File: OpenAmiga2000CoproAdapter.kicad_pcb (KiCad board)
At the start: 2 copper layers, 188.6 x 110.4 mm, 74 parts, among them CN1 A2000_COPRO_SLOT, P1 CONN_2, P10 CONN_1, P11 CONN_1, P12 CONN_1, P13 CONN_1, P14 CONN_1, P15 CONN_1, P2 CONN_2, P3 CONN_2, P4 CONN_2, P5 CONN_1, P6 CONN_1, P7 CONN_1, P8 CONN_1, P9 CONN_1, P99 OSHW_LOGO, U1 68000D, U10 Spare, U11 74HCT00, U12 74HCT27, U13 74HCT74, U14 74F86, U15 74F74, U16 74HCT04, U17 74HCT112, U18 74F157, U19 74F157, U2 AS6C4008-55PCN, U3 AS6C4008-55PCN, U4 AS6C4008-55PCN, U5 AS6C4008-55PCN, U6 74HCT00, U7 74HCT32, U8 74HCT32, U9 74LS05

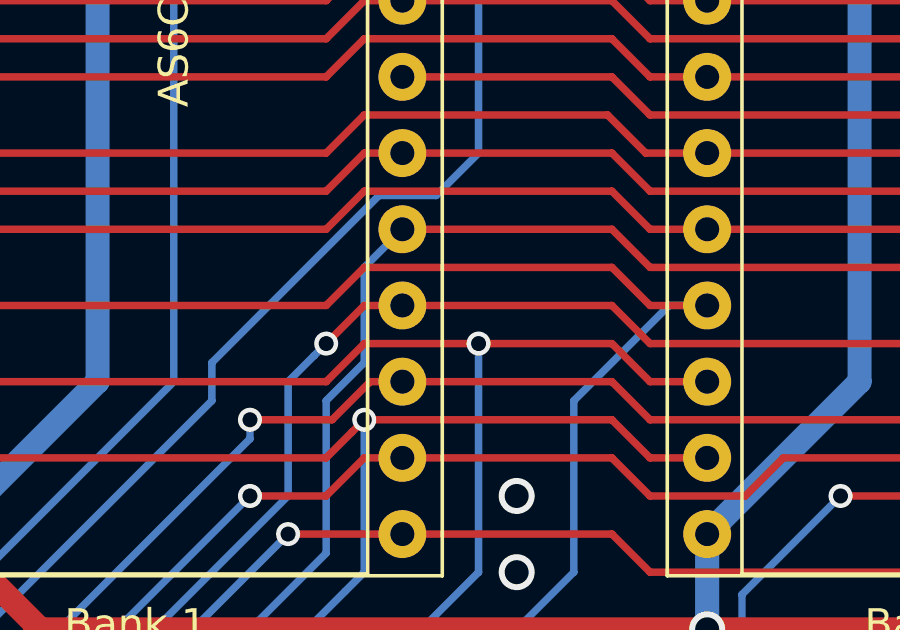
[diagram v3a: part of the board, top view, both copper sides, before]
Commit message: remove via
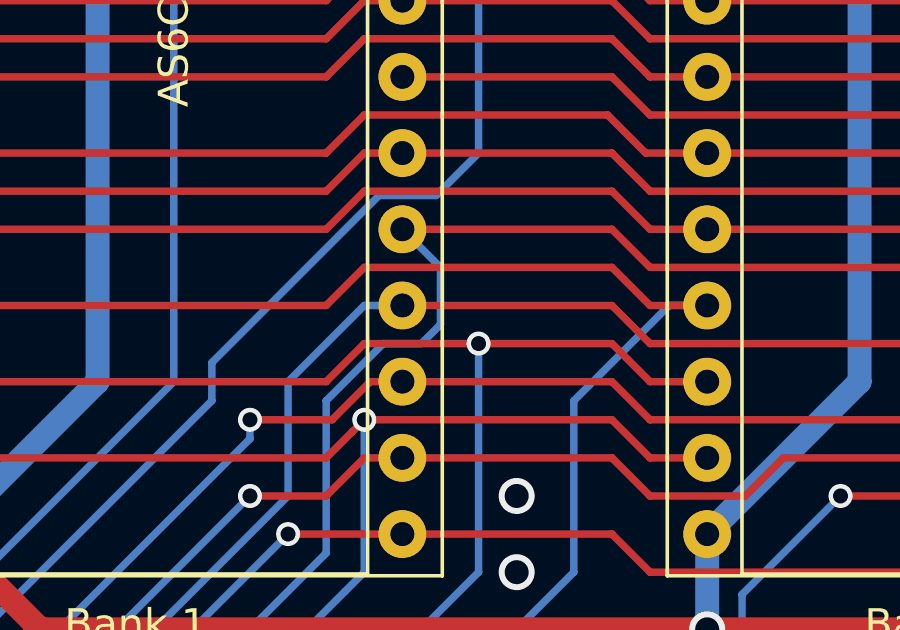
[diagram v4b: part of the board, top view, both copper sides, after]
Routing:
- net /d7: track 89.9 -> 91.7 mm
- net /d6: vias 2 -> 1
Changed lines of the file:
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@@
   (segment (start 95.758 139.1845) (end 95.758 134.9375) (width 0.25) (layer F.Cu) (net 60) (status 20))
   (segment (start 95.758 142.6845) (end 95.758 139.1845) (width 0.25) (layer F.Cu) (net 60) (status 10))
-  (via (at 100.901502 86.36) (size 0.8) (drill 0.5) (layers F.Cu B.Cu) (net 60))
-  (segment (start 99.6315 87.630002) (end 100.501503 86.759999) (width 0.25) (layer B.Cu) (net 60))
-  (segment (start 99.6315 91.44) (end 99.6315 87.630002) (width 0.25) (layer B.Cu) (net 60))
-  (segment (start 100.501503 86.759999) (end 100.901502 86.36) (width 0.25) (layer B.Cu) (net 60))
-  (segment (start 94.53299 96.53851) (end 99.6315 91.44) (width 0.25) (layer B.Cu) (net 60))
-  (segment (start 94.53299 97.17351) (end 94.53299 96.53851) (width 0.25) (layer B.Cu) (net 60))
   (via (at 94.53299 97.17351) (size 0.8) (drill 0.5) (layers F.Cu B.Cu) (net 60))
   (segment (start 95.758 115.5065) (end 95.758 134.9375) (width 0.25) (layer F.Cu) (net 60))
   (segment (start 94.53299 114.28149) (end 95.758 115.5065) (width 0.25) (layer F.Cu) (net 60))
   (segment (start 94.53299 97.17351) (end 94.53299 114.28149) (width 0.25) (layer F.Cu) (net 60))
-  (segment (start 102.171502 85.09) (end 100.901502 86.36) (width 0.25) (layer F.Cu) (net 60))
-  (segment (start 110.4265 85.09) (end 102.171502 85.09) (width 0.25) (layer F.Cu) (net 60))
-  (segment (start 111.6965 86.36) (end 110.4265 85.09) (width 0.25) (layer F.Cu) (net 60))
-  (segment (start 127.5715 86.36) (end 111.6965 86.36) (width 0.25) (layer F.Cu) (net 60))
-  (segment (start 128.8415 85.09) (end 127.5715 86.36) (width 0.25) (layer F.Cu) (net 60))
   (segment (start 98.298 139.1845) (end 98.298 134.9375) (width 0.25) (layer F.Cu) (net 61) (status 20))
   (segment (start 98.298 142.6845) (end 98.298 139.1845) (width 0.25) (layer F.Cu) (net 61) (status 10))
-  (segment (start 102.1715 86.995) (end 102.1715 83.82) (width 0.25) (layer B.Cu) (net 61))
-  (segment (start 100.9015 88.265) (end 102.1715 86.995) (width 0.25) (layer B.Cu) (net 61))
-  (segment (start 100.9015 93.345) (end 100.9015 88.265) (width 0.25) (layer B.Cu) (net 61))
   (segment (start 96.98301 97.26349) (end 97.0915 97.155) (width 0.25) (layer B.Cu) (net 61))
-  (segment (start 102.1715 83.82) (end 103.4415 82.55) (width 0.25) (layer B.Cu) (net 61))
-  (segment (start 97.0915 97.155) (end 100.9015 93.345) (width 0.25) (layer B.Cu) (net 61))
   (via (at 97.0915 97.155) (size 0.8) (drill 0.5) (layers F.Cu B.Cu) (net 61))
   (segment (start 98.298 115.5065) (end 98.298 134.9375) (width 0.25) (layer F.Cu) (net 61))
@@
   (segment (start 187.8965 40.005) (end 64.7065 40.005) (width 0.25) (layer B.Cu) (net 58))
   (segment (start 57.0865 81.025002) (end 59.246498 83.185) (width 0.25) (layer B.Cu) (net 58))
+  (segment (start 110.4265 85.09) (end 103.4415 85.09) (width 0.25) (layer F.Cu) (net 60))
+  (segment (start 111.6965 86.36) (end 110.4265 85.09) (width 0.25) (layer F.Cu) (net 60))
+  (segment (start 127.5715 86.36) (end 111.6965 86.36) (width 0.25) (layer F.Cu) (net 60))
+  (segment (start 128.8415 85.09) (end 127.5715 86.36) (width 0.25) (layer F.Cu) (net 60))
+  (segment (start 102.171502 85.09) (end 103.4415 85.09) (width 0.25) (layer B.Cu) (net 60))
+  (segment (start 99.6315 87.630002) (end 102.171502 85.09) (width 0.25) (layer B.Cu) (net 60))
+  (segment (start 99.6315 91.44) (end 99.6315 87.630002) (width 0.25) (layer B.Cu) (net 60))
+  (segment (start 94.53299 96.53851) (end 99.6315 91.44) (width 0.25) (layer B.Cu) (net 60))
+  (segment (start 94.53299 97.17351) (end 94.53299 96.53851) (width 0.25) (layer B.Cu) (net 60))
+  (segment (start 104.7115 83.82) (end 103.4415 82.55) (width 0.25) (layer B.Cu) (net 61))
+  (segment (start 104.0765 86.36) (end 104.7115 85.725) (width 0.25) (layer B.Cu) (net 61))
+  (segment (start 102.8065 86.36) (end 104.0765 86.36) (width 0.25) (layer B.Cu) (net 61))
+  (segment (start 100.9015 88.265) (end 102.8065 86.36) (width 0.25) (layer B.Cu) (net 61))
+  (segment (start 104.7115 85.725) (end 104.7115 83.82) (width 0.25) (layer B.Cu) (net 61))
+  (segment (start 100.9015 93.345) (end 100.9015 88.265) (width 0.25) (layer B.Cu) (net 61))
+  (segment (start 97.0915 97.155) (end 100.9015 93.345) (width 0.25) (layer B.Cu) (net 61))
   (via (at 135.1915 98.425) (size 0.8) (drill 0.5) (layers F.Cu B.Cu) (net 64))
   (segment (start 139.0015 87.63) (end 135.1915 91.44) (width 0.25) (layer B.Cu) (net 64))

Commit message: move track
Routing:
- net GND: vias 128 -> 130
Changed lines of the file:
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@@
     (thickness 1.6)
     (drawings 124)
-    (tracks 2292)
+    (tracks 2295)
     (zones 0)
     (modules 74)
@@
   (via (at 108.5215 109.22) (size 1.2) (drill 0.8) (layers F.Cu B.Cu) (net 1))
   (via (at 105.9815 100.965) (size 1.2) (drill 0.8) (layers F.Cu B.Cu) (net 1))
-  (via (at 105.9815 109.855) (size 1.2) (drill 0.8) (layers F.Cu B.Cu) (net 1))
+  (via (at 105.9815 109.22) (size 1.2) (drill 0.8) (layers F.Cu B.Cu) (net 1))
   (via (at 144.0815 95.885) (size 1.2) (drill 0.8) (layers F.Cu B.Cu) (net 1))
   (via (at 141.5415 95.885) (size 1.2) (drill 0.8) (layers F.Cu B.Cu) (net 1))
@@
   (via (at 144.0815 127.635) (size 1.2) (drill 0.8) (layers F.Cu B.Cu) (net 1))
   (via (at 141.5415 130.175) (size 1.2) (drill 0.8) (layers F.Cu B.Cu) (net 1))
-  (via (at 136.4615 107.95) (size 1.2) (drill 0.8) (layers F.Cu B.Cu) (net 1))
+  (via (at 133.9215 109.22) (size 1.2) (drill 0.8) (layers F.Cu B.Cu) (net 1))
   (via (at 213.9315 103.505) (size 1.2) (drill 0.8) (layers F.Cu B.Cu) (net 1))
   (segment (start 213.9315 62.23) (end 213.9315 62.795685) (width 0.8) (layer B.Cu) (net 1))
@@
   (via (at 224.0915 47.625) (size 1.2) (drill 0.8) (layers F.Cu B.Cu) (net 1))
   (via (at 224.7265 71.12) (size 1.2) (drill 0.8) (layers F.Cu B.Cu) (net 1))
+  (via (at 136.4615 108.585) (size 0.8) (drill 0.5) (layers F.Cu B.Cu) (net 1))
+  (via (at 116.1415 109.22) (size 1.2) (drill 0.8) (layers F.Cu B.Cu) (net 1))
   (via (at 118.0465 91.44) (size 0.8) (drill 0.5) (layers F.Cu B.Cu) (net 127))
   (segment (start 131.318 134.9375) (end 131.318 131.806498) (width 0.8) (layer F.Cu) (net 2))
@@
   (via (at 152.9715 106.68) (size 0.8) (drill 0.5) (layers F.Cu B.Cu) (net 74))
   (segment (start 151.7015 85.09) (end 151.7015 105.41) (width 0.25) (layer B.Cu) (net 74))
-  (segment (start 118.64448 106.68) (end 152.9715 106.68) (width 0.25) (layer F.Cu) (net 74))
-  (segment (start 117.39299 107.93149) (end 118.64448 106.68) (width 0.25) (layer F.Cu) (net 74))
+  (segment (start 118.00948 107.315) (end 152.3365 107.315) (width 0.25) (layer F.Cu) (net 74))
+  (segment (start 152.3365 107.315) (end 152.9715 106.68) (width 0.25) (layer F.Cu) (net 74))
+  (segment (start 117.39299 107.93149) (end 118.00948 107.315) (width 0.25) (layer F.Cu) (net 74))
   (segment (start 117.39299 113.64649) (end 117.39299 107.93149) (width 0.25) (layer F.Cu) (net 74))
   (segment (start 118.618 114.8715) (end 117.39299 113.64649) (width 0.25) (layer F.Cu) (net 74))

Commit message: description
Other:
- board text added: "Amiga 2000 14MHz Accelerator 2MB Fast RAM / ROM Emulation"
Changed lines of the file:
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@@
   (general
     (thickness 1.6)
-    (drawings 124)
+    (drawings 125)
     (tracks 2295)
     (zones 0)
@@
       (net 111 +12V))
   )
-  (gr_text "Little Turbo" (at 118.0465 38.1) (layer F.SilkS)
+  (gr_text "Amiga 2000 14MHz Accelerator\n2MB Fast RAM / ROM Emulation" (at 112.9665 42.545) (layer F.SilkS)
+    (effects (font (size 1 1) (thickness 0.15)))
+  )
+  (gr_text "Little Turbo" (at 112.9665 38.735) (layer F.SilkS)
     (effects (font (size 2 2) (thickness 0.15)))
   )
@@
     (effects (font (size 1 1) (thickness 0.15)))
   )
-  (gr_text "Jan Hofmeier 2021" (at 168.2115 38.1) (layer F.SilkS)
+  (gr_text "Jan Hofmeier 2021" (at 168.2115 38.735) (layer F.SilkS)
     (effects (font (size 2 2) (thickness 0.15)))
   )
@@
   (via (at 219.0115 114.3) (size 1.2) (drill 0.8) (layers F.Cu B.Cu) (net 1))
   (via (at 219.6465 120.015) (size 1.2) (drill 0.8) (layers F.Cu B.Cu) (net 1))
-  (via (at 125.6665 43.18) (size 1.2) (drill 0.8) (layers F.Cu B.Cu) (net 1))
-  (via (at 100.9015 43.18) (size 1.2) (drill 0.8) (layers F.Cu B.Cu) (net 1))
+  (via (at 126.3015 42.545) (size 1.2) (drill 0.8) (layers F.Cu B.Cu) (net 1))
+  (via (at 99.6315 42.545) (size 1.2) (drill 0.8) (layers F.Cu B.Cu) (net 1))
   (via (at 166.9415 59.69) (size 1.2) (drill 0.8) (layers F.Cu B.Cu) (net 1))
   (via (at 174.5615 59.69) (size 1.2) (drill 0.8) (layers F.Cu B.Cu) (net 1))

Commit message: add revision
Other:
- board text added: "Rev. 1.0"
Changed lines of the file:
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@@
   (general
     (thickness 1.6)
-    (drawings 125)
+    (drawings 126)
     (tracks 2295)
     (zones 0)
@@
   (page A4)
   (title_block
-    (title OpenAmiga2000CoproAdapter)
+    (title "Little Turbo")
     (date 2019-03-21)
-    (rev 3)
+    (rev 1.0)
     (company "Jan Hofmeier")
     (comment 1 "Based on work by Kipper2K, SukkoPera, Livio Plos and Jörg Richter")
     (comment 2 "Licensed under CERN OHL v.1.2")
+    (comment 3 "Amiga 2000 14MHz Accelerator")
+    (comment 4 "2MB Fast RAM / ROM Emulation")
   )
   (layers
@@
     (descr "14-lead though-hole mounted DIP package, row spacing 7.62 mm (300 mils)")
     (tags "THT DIP DIL PDIP 2.54mm 7.62mm 300mil")
-    (fp_text reference U11 (at 3.81 -2.33) (layer F.SilkS)
+    (fp_text reference U11 (at 3.81 17.78) (layer F.SilkS)
       (effects (font (size 1 1) (thickness 0.15)))
     )
@@
       (net 111 +12V))
   )
+  (gr_text "Rev. 1.0" (at 112.3315 45.72) (layer F.SilkS)
+    (effects (font (size 1 1) (thickness 0.15)))
+  )
   (gr_text "Amiga 2000 14MHz Accelerator\n2MB Fast RAM / ROM Emulation" (at 112.9665 42.545) (layer F.SilkS)
